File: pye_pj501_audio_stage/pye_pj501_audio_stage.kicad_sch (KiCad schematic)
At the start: 21 parts, among them T2 PYE_PJ105, U1 EL41, U2 ECH81

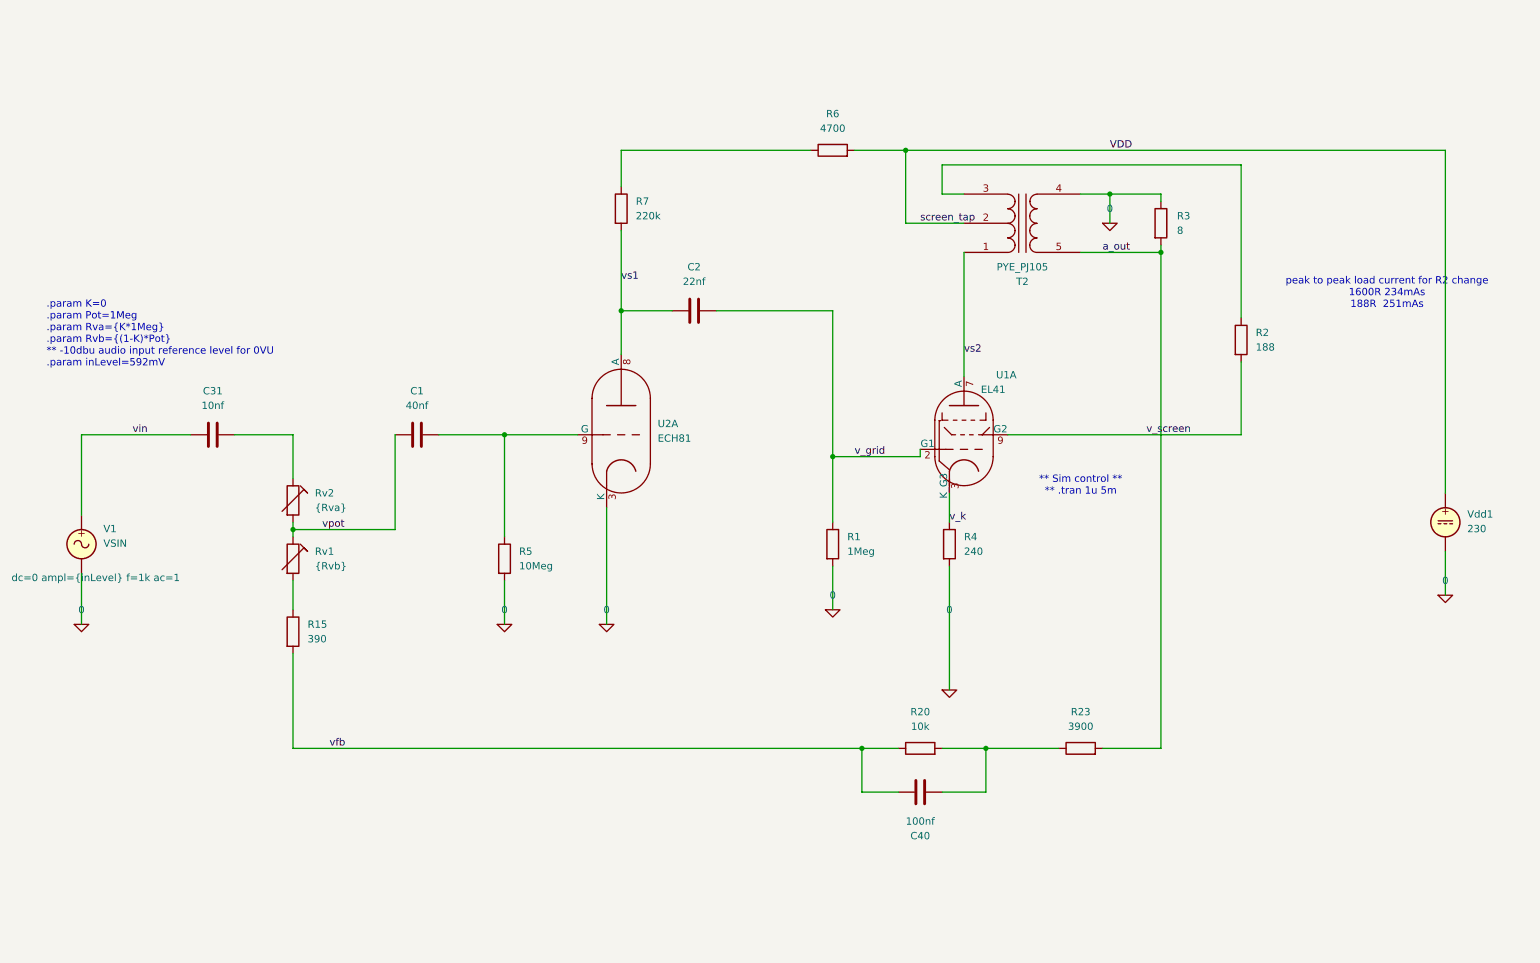
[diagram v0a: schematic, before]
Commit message: added front end pre-amp section
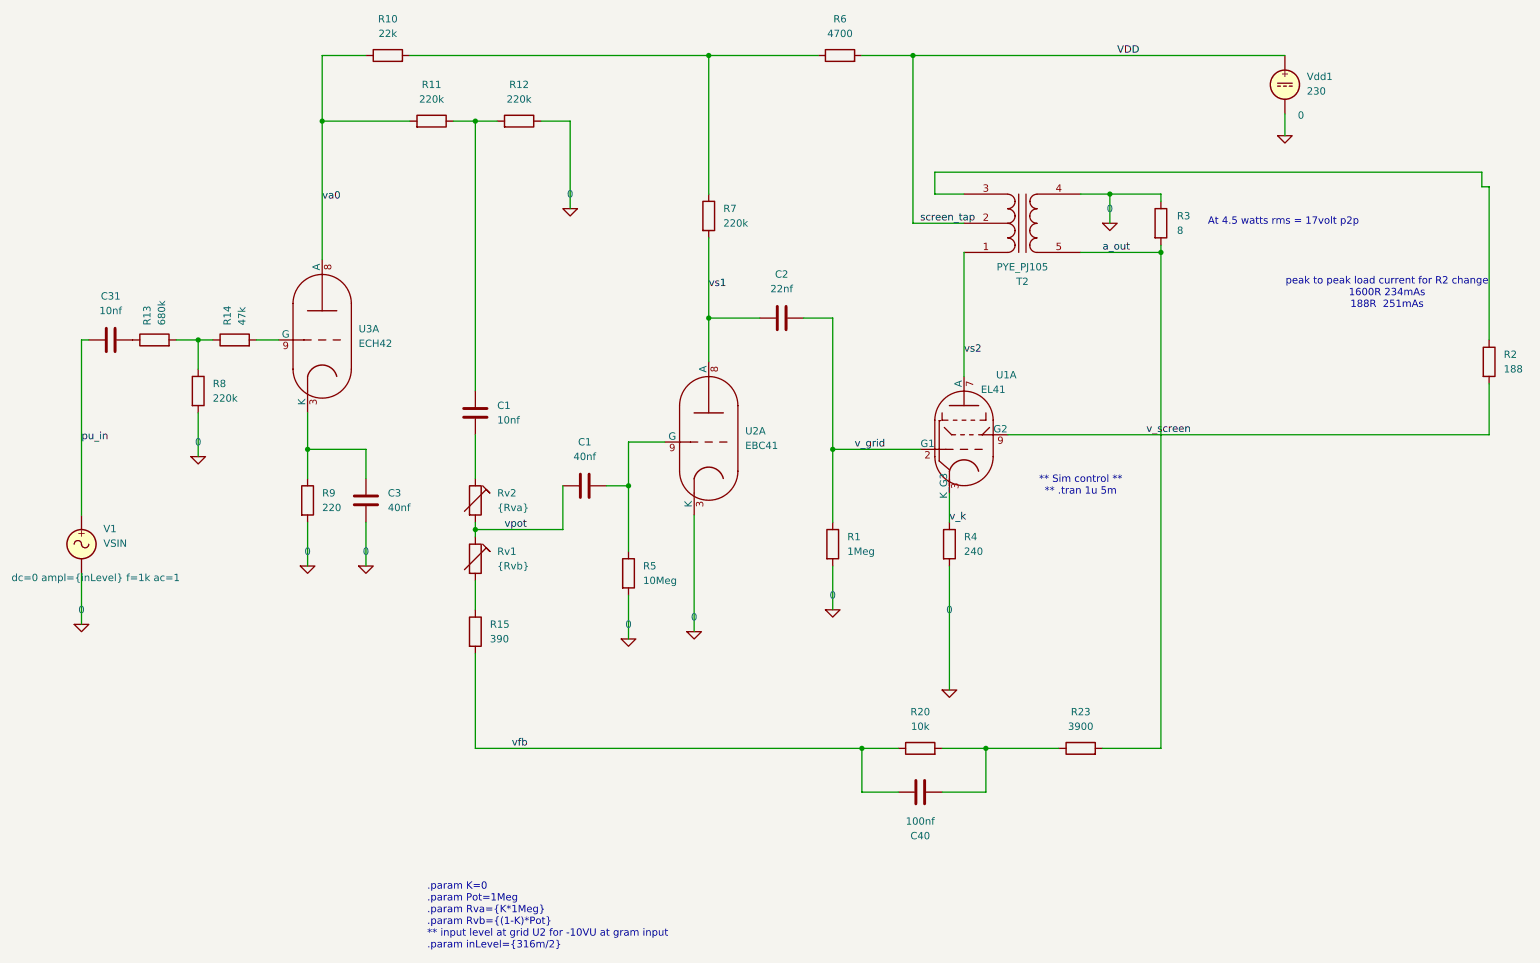
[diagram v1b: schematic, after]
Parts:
- added C1: 10nf, symbol Device:C
- added C3: 40nf, symbol Device:C
- added R10: 22k, symbol Device:R
- added R11, R12, R8: 220k, symbol Device:R
- added R13: 680k, symbol Device:R
- added R14: 47k, symbol Device:R
- added R9: 220, symbol Device:R
- added U3: ECH42, Valve:Valve_Noval_P, symbol Valve:ECH81
- U2: value ECH81 -> EBC41
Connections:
- net 0: now also C3.1, R12.1, R8.2, R9.2
- net at R6.1, R7.1: now also R10.2
- net at C31.2: now also R13.1; no longer Rv2.1
- net vin renamed pu_in
- new net: C3.2, R9.1, U3.3 (K)
- new net: R14.2, U3.9 (G)
- new net: C1.2, R11.1, R12.2
- new net: C1.1, Rv2.1
- new net: R13.2, R14.1, R8.1
- new net va0: R10.1, R11.2, U3.8 (A)
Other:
- note added: ".param K=0 .param Pot=1Meg .param Rva={K*1Meg} .param Rvb={(1-K)*Pot} ** input level at grid U2 for -10VU at gram input .param inLevel={316m/2}"
- note added: "At 4.5 watts rms = 17volt p2p"
- note removed: ".param K=0 .param Pot=1Meg .param Rva={K*1Meg} .param Rvb={(1-K)*Pot} ** -10dbu audio input reference level for 0VU .param inLevel=592mV"
- moved on the sheet: C1, C2, C31, R15, R2, R5, R6, R7, Rv1, Rv2, U2A, Vdd1
